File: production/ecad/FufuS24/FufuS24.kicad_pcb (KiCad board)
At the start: 4 copper layers, 120 x 120 mm, 146 parts, among them IC1 NLVPCA9535EDTR2G, J1 Conn_01x02, J10 691137710002, J12 691137710002, J13 5033950410, J2 Conn_01x02, J3 HDMI_A, J4 USB_B_Micro, J5 691137710004, J6 5025840270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

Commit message: if you're reading this aaaaaaa
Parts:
- removed C40, C41, C42, C43, C44, C45, C46, C47: 100nF, footprints:CAPC2012X94N
- removed D1, D2: D_Schottky, footprints:ShocktyDiode0805
- removed J3: HDMI_A, footprints:HDMI_A
- removed J4: USB_B_Micro, footprints:USB_Micro
- removed R21, R22, R23, R24, R25, R26, R27, R28: 5.6, footprints:RESC2012X60N
- removed U10, U11: TPD4E1U06DBVR, footprints:TPD4E1U06DBVR_footprint
- removed U3: TPD2E001DRLR, footprints:QFN-FCMOD_365R6FRDN_TEX
- added D8: D_Schottky, Diode_SMD:D_SMA, F.Cu at (138.6, 39.6)
- added J11: USB_B_Micro, Connector_USB:USB_Micro-B_Molex-105017-0001, F.Cu at (134.8, 32.7)
- added TH1: ~, Connector_PinSocket_2.54mm:PinSocket_1x11_P2.54mm_Vertical, F.Cu at (98.5, 33.1)
- added U13: TPD2E001DRLR, Package_TO_SOT_SMD:Texas_R-PDSO-N5_DRL-5, F.Cu at (133.8, 39.5)
- C10, C2, C3, C8, R5, Y1: moved to B.Cu
- C11, C12, C13, C14, C15, C16, C6, C7, C9: footprint footprints:CAPC2012X94N -> footprints:WCAP-CSGP_885012206026; moved to B.Cu
- C39: footprint footprints:CAPC2012X94N -> Capacitor_SMD:C_0805_2012Metric
- moved C39 39.5 mm to (138.6, 45.5), turned to 90 degrees
- moved C8 22.7 mm to (151.7, 84.0)
- moved R5 16.9 mm to (149.4, 96.2), turned to 180 degrees
- moved C2 2.95 mm to (142.7, 102.2), turned to 180 degrees
- moved Y1 2.39 mm to (138.7, 97.9)
- moved C3 2.35 mm to (134.8, 102.2), turned to 180 degrees
- moved U2 1.36 mm to (146.8, 78.3)
- turned C10 to 180 degrees
- turned C11 to 180 degrees
- turned C12 to 180 degrees
- turned C13 to 180 degrees
- turned C14 to 180 degrees
- turned C15 to 180 degrees
- turned C16 to 180 degrees
- turned C6 to 180 degrees
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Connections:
- C39 pad 1: DVI_D2+ -> GNDREF
- C39 pad 2: Net-(U11-D2+) -> +5V
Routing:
- net Net-(C3-Pad2): track 0.00 -> 38.0 mm
- net +3.3V: track 33.1 -> 12.6 mm, vias 2 -> 7
- net Net-(U1-XIN): track 0.00 -> 10.7 mm, vias 0 -> 1
- net GNDREF: track 2.13 -> 5.97 mm, vias 54 -> 56
- net Net-(U1-XOUT): track 0.00 -> 3.73 mm, vias 0 -> 1

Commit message: Layout update 3/15 morning
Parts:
- C2, C3, R5, Y1: moved to F.Cu
- moved C16 43.2 mm to (145.2, 81.5), turned to 90 degrees
- moved R1 42.4 mm to (187.3, 80.1), turned to 180 degrees
- moved R41 42.0 mm to (148.7, 66.7)
- moved R3 42.0 mm to (150.8, 72.5)
- moved R4 42.0 mm to (150.7, 75.2)
- moved R42 42.0 mm to (151.5, 66.7)
- moved C15 39.8 mm to (146.8, 81.5), turned to 90 degrees
- moved C14 36.2 mm to (148.3, 81.5), turned to 90 degrees
- moved C13 33.5 mm to (149.9, 81.5), turned to 90 degrees
- moved C12 30.5 mm to (151.4, 81.5), turned to 90 degrees
- moved C10 27.4 mm to (140.7, 87.0)
- moved C11 27.2 mm to (153.0, 81.5), turned to 90 degrees
- moved C9 23.9 mm to (154.6, 81.5), turned to 90 degrees
- moved C3 15.7 mm to (148.6, 109.6), turned to -90 degrees
- moved C7 10.4 mm to (149.8, 97.4), turned to 0 degrees
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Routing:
- net Watersense1_Mode: track 0.00 -> 45.5 mm, vias 0 -> 2
- net Watersense2_Mode: track 0.00 -> 45.0 mm, vias 0 -> 2
- net Watersense1_Read: track 0.00 -> 44.2 mm
- net Watersense2_Read: track 0.00 -> 43.6 mm
- net Net-(C3-Pad2): track 38.0 -> 3.96 mm
- net Net-(U1-QSPI_SS): track 0.00 -> 30.6 mm
- net AD2_EXT: track 0.00 -> 25.7 mm, vias 0 -> 2
- net Net-(U1-QSPI_SD1): track 0.00 -> 24.0 mm
- net AD1_EXT: track 0.00 -> 22.8 mm, vias 0 -> 2
- net Net-(U1-QSPI_SD2): track 0.00 -> 22.5 mm
- net +3.3V: track 12.6 -> 34.6 mm, vias 7 -> 8
- net AD0_EXT: track 0.00 -> 14.2 mm
- net SCL_EXT: track 0.00 -> 14.1 mm
- net SDA_EXT: track 0.00 -> 14.0 mm
- net Net-(U1-QSPI_SD3): track 0.00 -> 13.1 mm
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
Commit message: fixing traces
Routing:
- net Watersense1_Mode: track 45.5 -> 0.00 mm, vias 2 -> 0
- net Watersense2_Mode: track 45.0 -> 0.00 mm, vias 2 -> 0
- net Watersense1_Read: track 44.2 -> 0.00 mm
- net Watersense2_Read: track 43.6 -> 0.00 mm
- net +3.3V: track 34.6 -> 33.6 mm, vias 8 -> 7
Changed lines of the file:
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@@
   (segment (start 151.21 87.65) (end 151.765 87.65) (width 0.135) (layer "F.Cu") (net 20))
   (segment (start 144.34 87.65) (end 143.805 87.65) (width 0.135) (layer "F.Cu") (net 20))
-  (segment (start 151.21 91.25) (end 152.275 91.25) (width 0.135) (layer "F.Cu") (net 20))
   (segment (start 148.375 85.95) (end 148.175 85.75) (width 0.135) (layer "F.Cu") (net 20))
   (segment (start 149.975 85.875) (end 150.125 85.725) (width 0.2) (layer "F.Cu") (net 20))
@@
   (via (at 152.41 87.005) (size 0.6) (drill 0.2) (layers "F.Cu" "B.Cu") (free) (net 20))
   (via (at 150.125 85.725) (size 0.6) (drill 0.2) (layers "F.Cu" "B.Cu") (free) (net 20))
-  (via (at 152.275 91.25) (size 0.6) (drill 0.2) (layers "F.Cu" "B.Cu") (free) (net 20))
   (segment (start 145.2 82.3) (end 146.758333 82.3) (width 0.1348) (layer "B.Cu") (net 20))
   (segment (start 148.175 84.45) (end 149.874999 82.750001) (width 0.1348) (layer "B.Cu") (net 20))
@@
   (segment (start 168.924 35.81) (end 168.924 37.4536) (width 1) (layer "F.Cu") (net 67))
   (segment (start 168.924 37.4536) (end 174.6758 43.2054) (width 1) (layer "F.Cu") (net 67))
-  (segment (start 188.595 109.946001) (end 185.603999 109.946001) (width 0.1348) (layer "F.Cu") (net 70))
-  (segment (start 158.9 98.1) (end 152.6174 91.8174) (width 0.1348) (layer "F.Cu") (net 70))
-  (segment (start 185.575 109.975) (end 185.65 109.975) (width 0.1348) (layer "F.Cu") (net 70))
-  (segment (start 158.925 98.1) (end 158.9 98.1) (width 0.1348) (layer "F.Cu") (net 70))
-  (segment (start 152.039975 91.8174) (end 151.872575 91.65) (width 0.1348) (layer "F.Cu") (net 70))
-  (segment (start 184.025 107.8) (end 168.625 107.8) (width 0.1348) (layer "F.Cu") (net 70))
-  (segment (start 185.65 109.975) (end 185.675 109.95) (width 0.1348) (layer "F.Cu") (net 70))
-  (segment (start 152.6174 91.8174) (end 152.039975 91.8174) (width 0.1348) (layer "F.Cu") (net 70))
-  (segment (start 168.625 107.8) (end 158.925 98.1) (width 0.1348) (layer "F.Cu") (net 70))
-  (segment (start 151.872575 91.65) (end 151.21 91.65) (width 0.1348) (layer "F.Cu") (net 70))
-  (segment (start 185.603999 109.946001) (end 185.575 109.975) (width 0.1348) (layer "F.Cu") (net 70))
-  (via (at 184.025 107.8) (size 0.6) (drill 0.2) (layers "F.Cu" "B.Cu") (net 70))
-  (via (at 185.575 109.975) (size 0.6) (drill 0.2) (layers "F.Cu" "B.Cu") (net 70))
-  (segment (start 185.575 109.35) (end 184.025 107.8) (width 0.1348) (layer "B.Cu") (net 70))
-  (segment (start 185.575 109.975) (end 185.575 109.35) (width 0.1348) (layer "B.Cu") (net 70))
-  (segment (start 184.025 107.8) (end 184.05 107.825) (width 0.1348) (layer "B.Cu") (net 70))
-  (segment (start 151.704646 92.05) (end 151.21 92.05) (width 0.1348) (layer "F.Cu") (net 71))
-  (segment (start 188.595 108.446001) (end 168.100647 108.446001) (width 0.1348) (layer "F.Cu") (net 71))
-  (segment (start 168.100647 108.446001) (end 151.704646 92.05) (width 0.1348) (layer "F.Cu") (net 71))
-  (segment (start 153.7424 90.4174) (end 151.2426 90.4174) (width 0.1348) (layer "F.Cu") (net 72))
-  (segment (start 151.2426 90.4174) (end 151.21 90.45) (width 0.1348) (layer "F.Cu") (net 72))
-  (segment (start 154.55 91.225) (end 153.7424 90.4174) (width 0.1348) (layer "F.Cu") (net 72))
-  (segment (start 185.125 106.925) (end 185.128998 106.946002) (width 0.1348) (layer "F.Cu") (net 72))
-  (segment (start 188.595 106.946002) (end 185.125 106.925) (width 0.1348) (layer "F.Cu") (net 72))
-  (via (at 185.125 106.925) (size 0.6) (drill 0.2) (layers "F.Cu" "B.Cu") (net 72))
-  (via (at 154.55 91.225) (size 0.6) (drill 0.2) (layers "F.Cu" "B.Cu") (net 72))
-  (segment (start 154.55 91.225) (end 154.525 91.2) (width 0.1348) (layer "B.Cu") (net 72))
-  (segment (start 154.55 92.425) (end 154.55 91.225) (width 0.1348) (layer "B.Cu") (net 72))
-  (segment (start 185.125 106.925) (end 169.05 106.925) (width 0.1348) (layer "B.Cu") (net 72))
-  (segment (start 169.05 106.925) (end 154.55 92.425) (width 0.1348) (layer "B.Cu") (net 72))
-  (segment (start 151.7414 90.85) (end 151.21 90.85) (width 0.1348) (layer "F.Cu") (net 73))
-  (segment (start 152.6326 90.6826) (end 151.9088 90.6826) (width 0.1348) (layer "F.Cu") (net 73))
-  (segment (start 188.595 105.446) (end 167.396 105.446) (width 0.1348) (layer "F.Cu") (net 73))
-  (segment (start 151.9088 90.6826) (end 151.7414 90.85) (width 0.1348) (layer "F.Cu") (net 73))
-  (segment (start 167.396 105.446) (end 152.6326 90.6826) (width 0.1348) (layer "F.Cu") (net 73))
   (segment (start 185.625 90.975) (end 184.67 90.975) (width 0.5) (layer "F.Cu") (net 74))
   (segment (start 193.627801 90.125) (end 186.475 90.125) (width 0.5) (layer "F.Cu") (net 74))

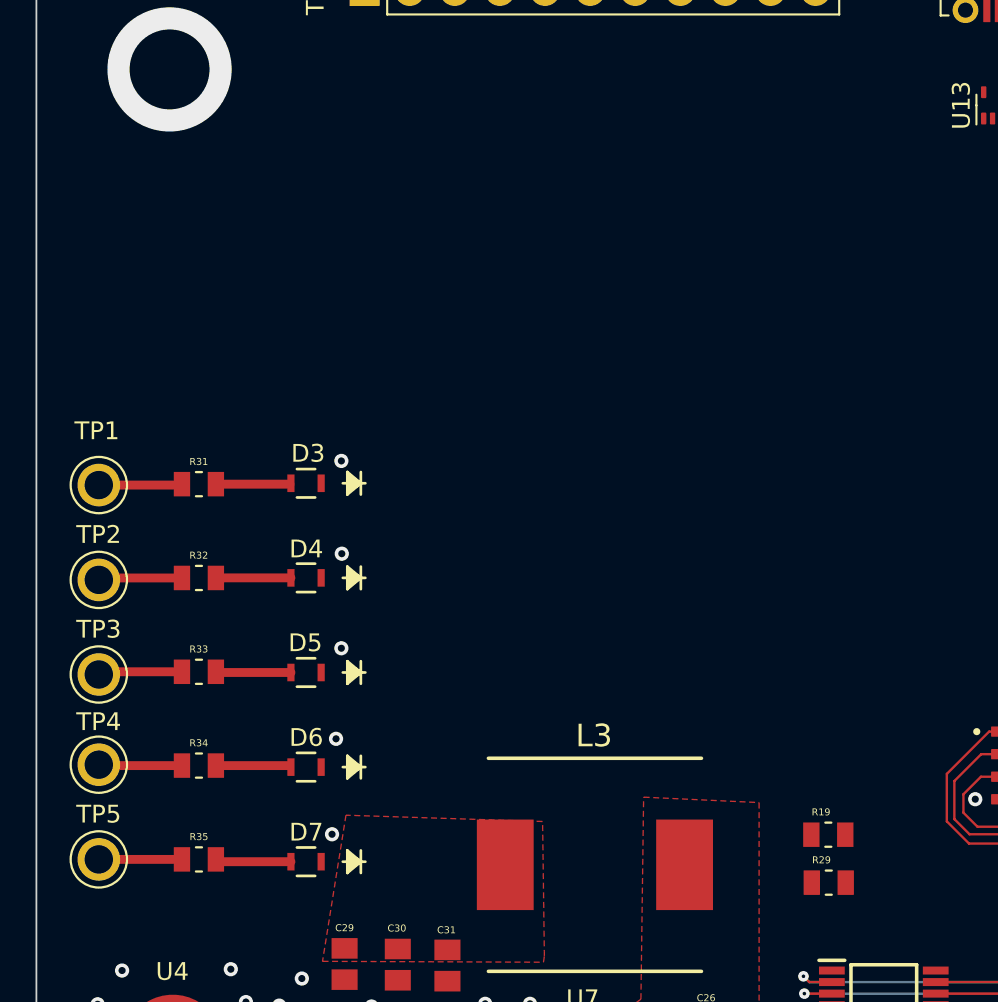
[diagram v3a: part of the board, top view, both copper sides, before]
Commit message: Component placement for piezo
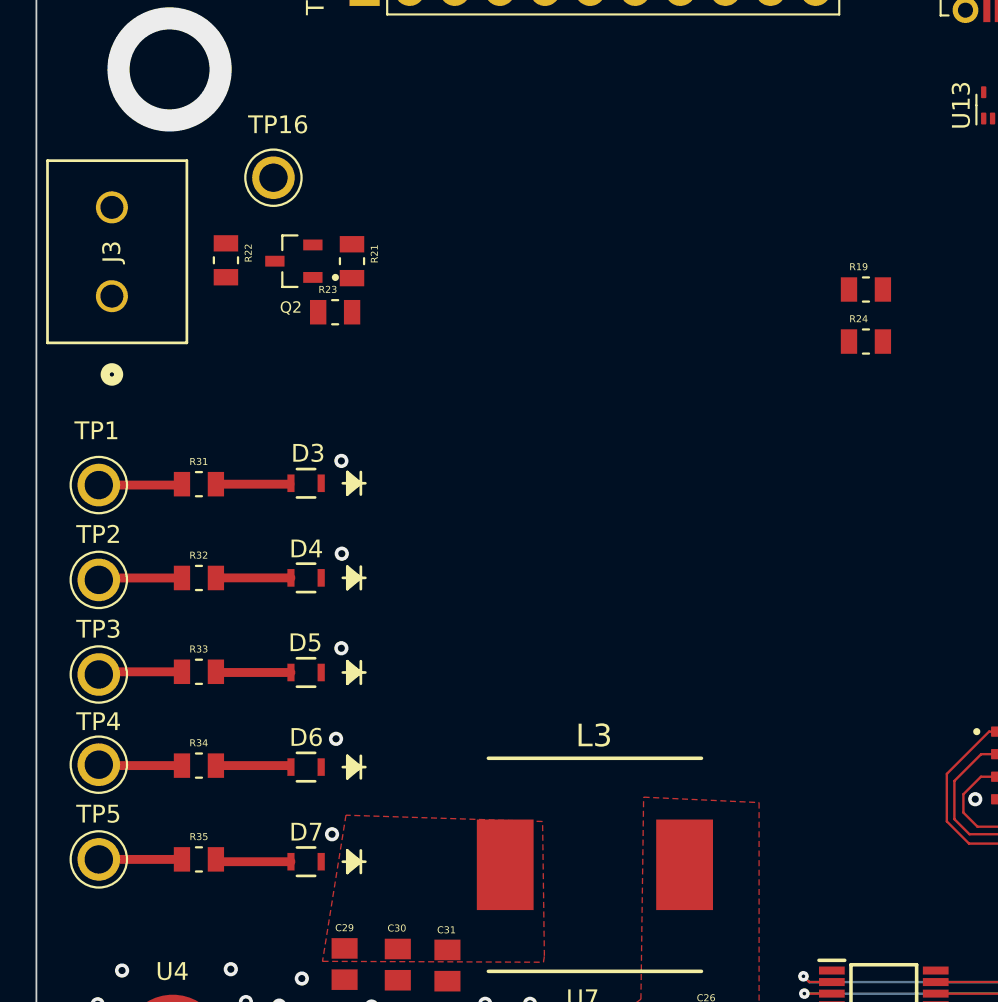
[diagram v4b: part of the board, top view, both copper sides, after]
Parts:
- removed R29: 4.7k, footprints:RESC2012X60N
- added J3: 691137710002, footprints:CONN2_710002_WRE, F.Cu at (84.3, 50.3)
- added Q2: DMG2302UK-7, footprints:DMG2302UK-7_Footprint, F.Cu at (94.5, 48.3)
- added R21: 100, footprints:RESC2012X60N, F.Cu at (97.8, 48.3)
- added R22: 1k, footprints:RESC2012X60N, F.Cu at (90.7, 48.2)
- added R23: 500, footprints:RESC2012X60N, F.Cu at (96.8, 51.2)
- added R24: 4.7k, footprints:RESC2012X60N, F.Cu at (126.7, 52.8)
- added TP16: 5014, footprints:TP_5014, F.Cu at (93.3, 43.6)
- moved R19 30.8 mm to (126.7, 49.9)
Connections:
- IC1 pad 10: unconnected-(IC1-IO0_6-Pad10) -> Watersense1_Mode
- IC1 pad 11: unconnected-(IC1-IO0_7-Pad11) -> Watersense1_Read
- IC1 pad 13: unconnected-(IC1-IO1_0-Pad13) -> Piezo_Enable
- IC1 pad 18: Heat_PWM1 -> unconnected-(IC1-IO1_5-Pad18)
- IC1 pad 19: I2C0_SCL -> unconnected-(IC1-IO1_6-Pad19)
- IC1 pad 20: I2C0_SDA -> unconnected-(IC1-IO1_7-Pad20)
- IC1 pad 8: unconnected-(IC1-IO0_4-Pad8) -> Watersense2_Mode
- IC1 pad 9: unconnected-(IC1-IO0_5-Pad9) -> Watersense2_Read
- J9 pad 1: I2C0_SCL -> SCL_EXT
- J9 pad 2: I2C0_SDA -> SDA_EXT
- R19 pad 2: I2C0_SDA -> SCL_EXT
- U1 pad 31: Watersense1_Read -> Heat_PWM1
- U1 pad 32: Watersense1_Mode -> unconnected-(U1-GPIO21-Pad32)
- U1 pad 34: Watersense2_Read -> unconnected-(U1-GPIO22-Pad34)
- U1 pad 35: Watersense2_Mode -> unconnected-(U1-GPIO23-Pad35)

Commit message: Big layout push
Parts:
- removed IC1: NLVPCA9535EDTR2G, footprints:SOP65P640X120-24N
- added R25: 10k, footprints:RESC2012X60N, F.Cu at (179.0, 97.5)
- added R26: 10k, footprints:RESC2012X60N, F.Cu at (179.0, 102.2)
- added R27: 10k, footprints:RESC2012X60N, F.Cu at (174.2, 97.5)
- added R28: 10k, footprints:RESC2012X60N, F.Cu at (174.2, 102.2)
- added TP15: 5014, footprints:TP_5014, F.Cu at (184.2, 125.5)
- added TP17: 5014, footprints:TP_5014, F.Cu at (167.5, 112.0)
- added TP18: 5014, footprints:TP_5014, F.Cu at (184.2, 132.0)
- C1, C27, C32, C34: footprint footprints:CAPC2012X94N -> Capacitor_SMD:C_1210_3225Metric
- C35: footprint footprints:CAPC2012X94N -> footprints:CAPRR2500W80L2800T1330H1990
- C4: footprint footprints:CAPC2012X94N -> footprints:CAP_ECQUA_41.0LX15.0TX30.0H_PAN
- R9: footprint footprints:RESC2012X60N -> footprints:RES_SQP500_22X9P5_YAG
- moved Y1 52.8 mm to (114.0, 62.5)
- moved C3 52.1 mm to (118.2, 67.2), turned to 90 degrees
- moved C2 52.0 mm to (118.2, 59.4), turned to 90 degrees
- moved R5 44.9 mm to (118.2, 63.8), turned to 90 degrees
- moved C6 43.9 mm to (121.5, 62.2)
- moved C7 41.5 mm to (129.7, 61.0), turned to 180 degrees
- moved C11 38.8 mm to (124.2, 55.5), turned to -90 degrees
- moved U1 37.9 mm to (125.2, 59.8), turned to -90 degrees
- moved C8 36.5 mm to (121.4, 64.0)
- moved C12 35.4 mm to (127.5, 55.5), turned to -90 degrees
- moved C15 33.6 mm to (121.0, 60.0), turned to 0 degrees
- moved C9 32.1 mm to (127.5, 64.2)
- moved C13 31.4 mm to (129.7, 57.5), turned to 180 degrees
- moved U13 30.7 mm to (151.1, 64.9)
- moved C39 30.7 mm to (155.8, 70.9)
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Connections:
- C35 pad 1: Net-(J1-Pin_1) -> Net-(J1-Pin_2)
- C35 pad 2: Net-(J1-Pin_2) -> Net-(J1-Pin_1)
- C4 pad 1: Net-(J1-Pin_2) -> Net-(J1-Pin_1)
- J13 pad 1: Watersense1_Mode -> /Water Dispensing/Watersense_Mode_2
- J13 pad 3: Watersense2_Mode -> /Water Dispensing/Watersense_Mode_1
- L1 pad 2: Net-(J1-Pin_2) -> Net-(J1-Pin_1)
- U1 pad 29: I2C1_SDA_DVI -> HOT_LED_POS
- U1 pad 30: I2C1_SCL_DVI -> HOT_LED_NEG
- U1 pad 32: unconnected-(U1-GPIO21-Pad32) -> Pump_Enable
- U1 pad 34: unconnected-(U1-GPIO22-Pad34) -> Watersense2_Read
- U1 pad 35: unconnected-(U1-GPIO23-Pad35) -> Watersense1_Read
- U1 pad 4: AD0_EXT -> Piezo_Enable
- U1 pad 5: AD1_EXT -> unconnected-(U1-GPIO3-Pad5)
- U1 pad 6: AD2_EXT -> Motor_BIN1
- U5 pad 10: (no net) -> GNDREF
- U5 pad 11: (no net) -> GNDREF
- U5 pad 12: (no net) -> GNDREF
- U5 pad 13: (no net) -> GNDREF
- U5 pad 14: (no net) -> GNDREF
- U5 pad 15: (no net) -> GNDREF
- U6 pad 10: (no net) -> GNDREF
- U6 pad 11: (no net) -> GNDREF
- U6 pad 12: (no net) -> GNDREF
- U6 pad 13: (no net) -> GNDREF
- U6 pad 14: (no net) -> GNDREF
- U6 pad 15: (no net) -> GNDREF
- U7 pad 10: (no net) -> GNDREF
- U7 pad 11: (no net) -> GNDREF
- U7 pad 12: (no net) -> GNDREF
- U7 pad 13: (no net) -> GNDREF
- U7 pad 14: (no net) -> GNDREF
- U7 pad 15: (no net) -> GNDREF
- U9 pad 2: Net-(J1-Pin_1) -> Net-(J1-Pin_2)
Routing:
- net Net-(J1-Pin_1): track 61.4 -> 0.00 mm, vias 1 -> 0
- net Net-(J1-Pin_2): track 52.7 -> 10.1 mm
- net AD2_EXT: track 25.7 -> 0.00 mm, vias 2 -> 0
- net AD1_EXT: track 22.8 -> 0.00 mm, vias 2 -> 0
- net /Water Dispensing/Watersense_Mode_2: track 0.00 -> 21.5 mm, vias 0 -> 2
- net /Induction Heating/VSS: track 34.1 -> 13.1 mm, vias 0 -> 1
- net GNDREF: track 5.97 -> 26.1 mm, vias 66 -> 61
- net Net-(U9-G): track 9.89 -> 27.7 mm
- net /Water Dispensing/Watersense_Mode_1: track 0.00 -> 15.3 mm
- net AD0_EXT: track 14.2 -> 0.00 mm
- net Net-(C51-Pad1): track 12.2 -> 0.00 mm
- net +3.3V: track 33.6 -> 40.4 mm, vias 7 -> 15
- net Net-(U7-FB): track 0.00 -> 6.34 mm
- net Net-(U8-CATHODE): track 3.02 -> 9.24 mm
- net Net-(U6-FB): track 0.28 -> 6.29 mm
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- added copper zone on B.Cu, net /Induction Heating/VSS
- added copper zone on B.Cu, net GNDREF
- added copper zone on F.Cu, net GNDREF
- added copper zone on F.Cu, net Net-(J1-Pin_1)
- removed copper zone on F.Cu, net Net-(U5-FB)
- removed copper zone on F.Cu, net Net-(U5-RT_SYNC)
- removed copper zone on F.Cu, net Net-(U6-FB)
- removed copper zone on F.Cu, net Net-(U7-FB)

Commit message: few more layout changes:
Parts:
- removed R41, R42: 1.75k, footprints:RESC2012X60N
- moved C39 35.5 mm to (138.2, 40.0)
- moved D8 32.0 mm to (142.8, 35.8), turned to 180 degrees
- moved U13 31.4 mm to (135.8, 37.5), turned to 180 degrees
- moved R4 17.5 mm to (135.2, 62.8), turned to 180 degrees
- moved R3 17.2 mm to (135.2, 60.8), turned to 180 degrees
- moved D11 9.97 mm to (150.5, 33.5)
- moved R45 9.97 mm to (150.5, 37.1)
- moved D10 7.97 mm to (155.8, 33.5)
- moved R44 7.97 mm to (155.7, 37.1)
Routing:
- net Piezo_Enable: track 0.00 -> 47.9 mm, vias 0 -> 1
- net USB_D-: track 0.00 -> 31.4 mm, vias 0 -> 2
- net USB_D+: track 0.00 -> 29.7 mm, vias 0 -> 2
- net GNDREF: track 26.1 -> 38.5 mm, vias 61 -> 68
- net Net-(Q2-D): track 0.00 -> 9.99 mm
- net +12V: track 18.7 -> 26.0 mm
- net +5V: track 16.3 -> 23.5 mm, vias 22 -> 26
- net Net-(U1-USB_DM): track 0.00 -> 6.27 mm
- net Net-(D8-A): track 0.00 -> 5.99 mm
- net Net-(U1-USB_DP): track 0.00 -> 5.61 mm
- net Net-(Q2-G): track 0.00 -> 4.31 mm
- net Motor_Step: track 0.00 -> 4.16 mm, vias 0 -> 1
- net Motor_DIR: track 0.00 -> 4.01 mm, vias 0 -> 1
- net Motor_BIN2: track 0.00 -> 2.65 mm, vias 0 -> 1
- net Net-(U12-~STALL): track 53.4 -> 55.4 mm
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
